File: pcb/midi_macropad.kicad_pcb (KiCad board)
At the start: 2 copper layers, 204.8 x 61.9 mm, 35 parts, among them J1 Conn_01x04_Pin, SW1 SW_Push, SW10 SW_Push, SW11 SW_Push, SW12 SW_Push, SW13 SW_Push, SW14 SW_Push, SW15 SW_Push, SW16 SW_Push, SW17 RotaryEncoder_Switch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

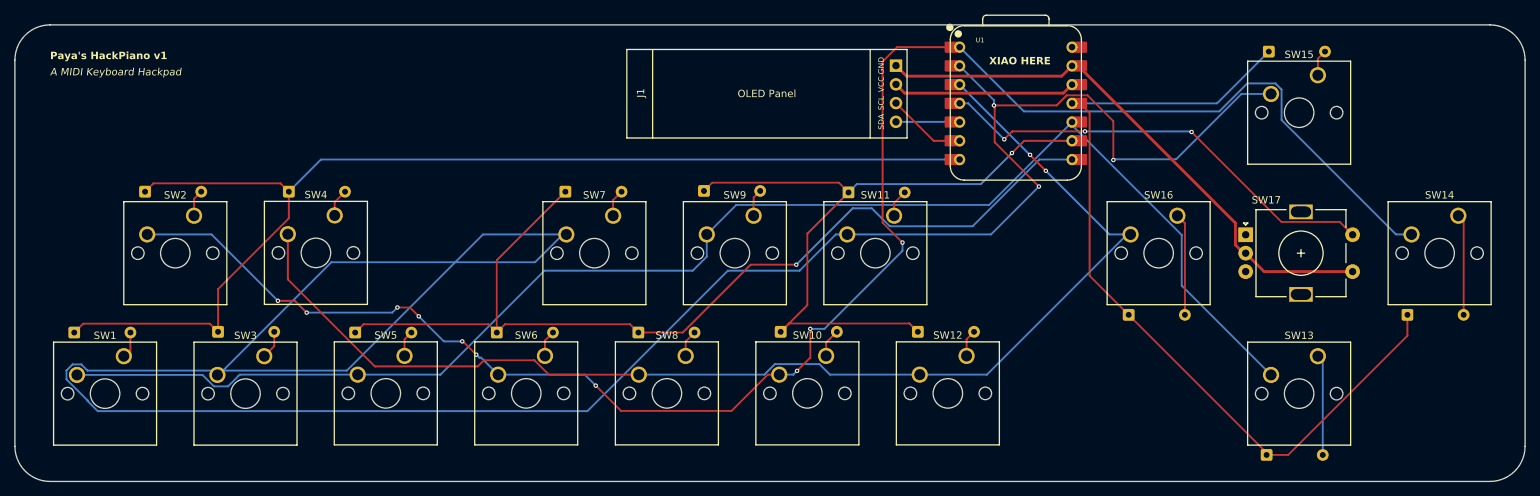
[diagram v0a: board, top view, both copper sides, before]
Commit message: fix: Change `edge.cuts` to a rectangle for easier measurement
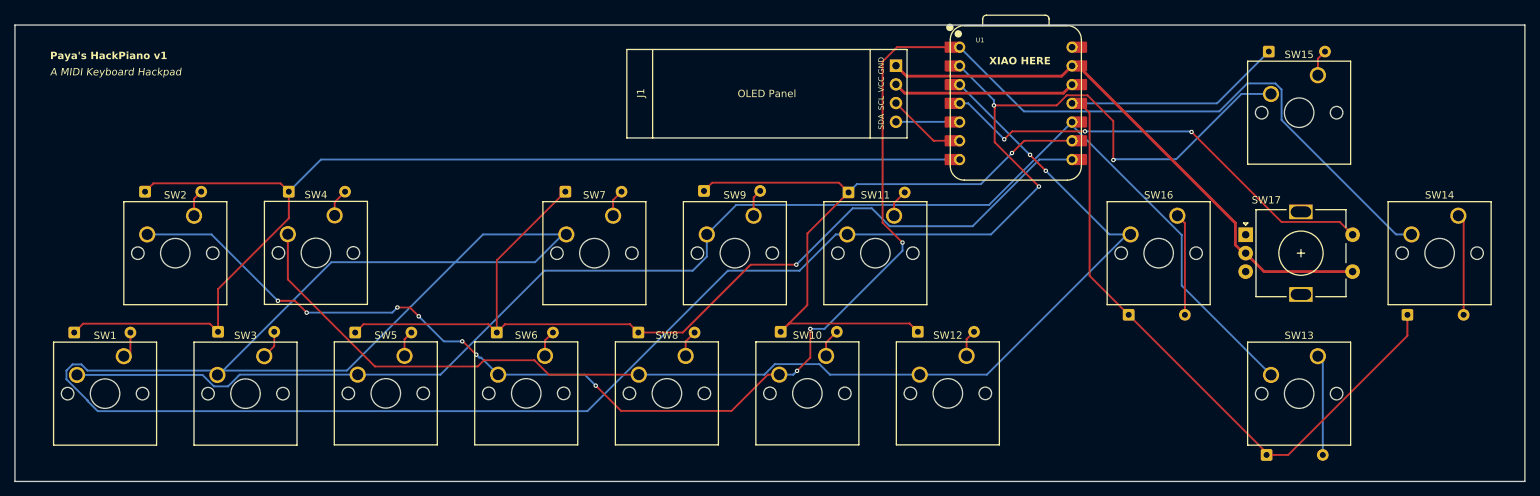
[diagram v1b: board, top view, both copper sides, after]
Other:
- outline, holes or cut-outs redrawn
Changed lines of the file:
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@@
 		)
 	)
-	(gr_arc
-		(start 38.1 140.49375)
-		(mid 34.732404 139.098846)
-		(end 33.3375 135.73125)
+	(gr_rect
+		(start 33.3375 78.6)
+		(end 238.1 140.49375)
 		(stroke
 			(width 0.05)
 			(type default)
 		)
+		(fill no)
 		(layer "Edge.Cuts")
 	)
-	(gr_arc
-		(start 33.3375 83.34375)
-		(mid 34.732404 79.976154)
-		(end 38.1 78.58125)
-		(stroke
-			(width 0.05)
-			(type default)
-		)
-		(layer "Edge.Cuts")
-	)
-	(gr_line
-		(start 38.1 78.58125)
-		(end 233.3625 78.58125)
-		(stroke
-			(width 0.05)
-			(type default)
-		)
-		(layer "Edge.Cuts")
-	)
-	(gr_line
-		(start 233.3625 140.49375)
-		(end 38.1 140.49375)
-		(stroke
-			(width 0.05)
-			(type default)
-		)
-		(layer "Edge.Cuts")
-	)
-	(gr_line
-		(start 33.3375 135.73125)
-		(end 33.3375 83.34375)
-		(stroke
-			(width 0.05)
-			(type default)
-		)
-		(layer "Edge.Cuts")
-	)
-	(gr_arc
-		(start 233.3625 78.58125)
-		(mid 236.730096 79.976154)
-		(end 238.125 83.34375)
-		(stroke
-			(width 0.05)
-			(type default)
-		)
-		(layer "Edge.Cuts")
-	)
-	(gr_line
-		(start 238.125 83.34375)
-		(end 238.125 135.73125)
-		(stroke
-			(width 0.05)
-			(type default)
-		)
-		(layer "Edge.Cuts")
-	)
-	(gr_arc
-		(start 238.125 135.73125)
-		(mid 236.730096 139.098846)
-		(end 233.3625 140.49375)
-		(stroke
-			(width 0.05)
-			(type default)
-		)
-		(layer "Edge.Cuts")
-	)
